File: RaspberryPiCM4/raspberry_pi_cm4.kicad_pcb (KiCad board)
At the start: 2 copper layers, 24 parts, among them J1 CONN_2x50_FEM_RPI_CM4_1-100, J2 CONN_2x50_FEM_RPI_CM4_101_200, U1 74LVC1G07_SOT353

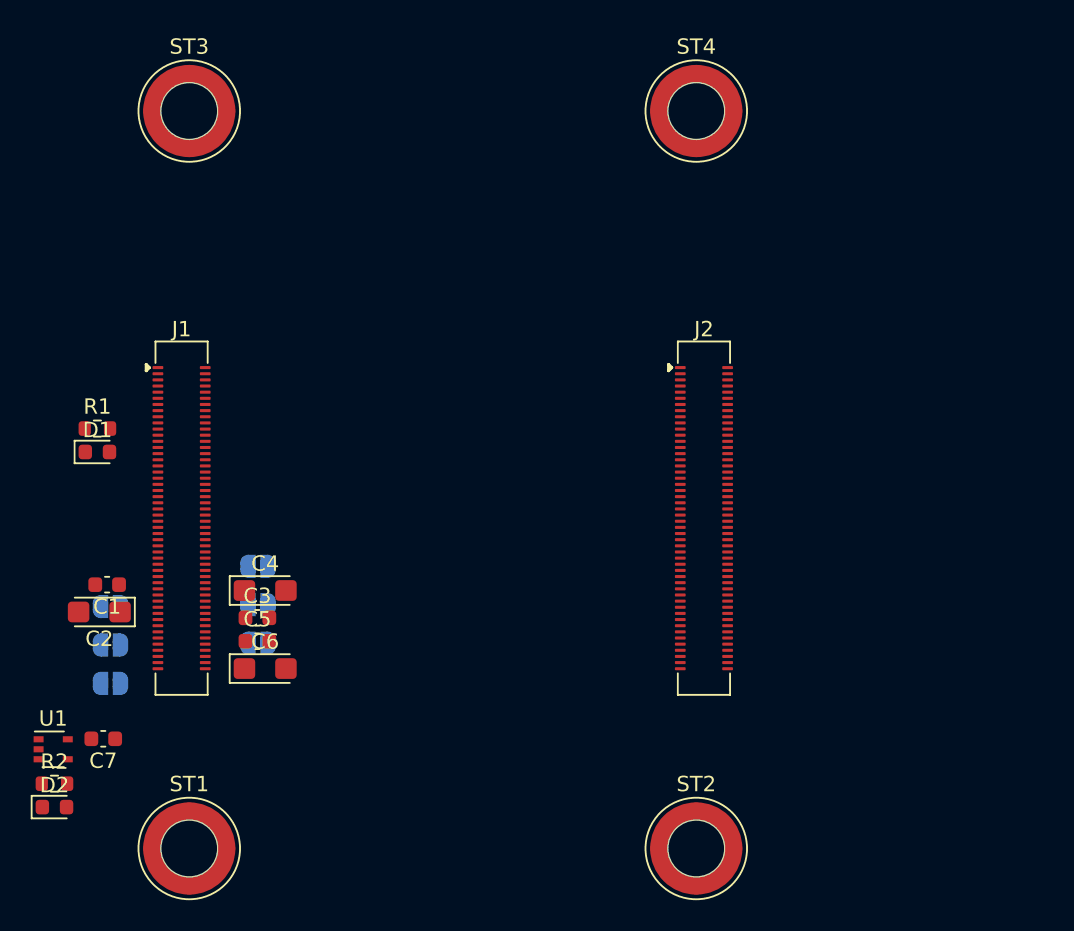
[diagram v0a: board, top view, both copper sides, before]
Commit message: migating to kicad 6
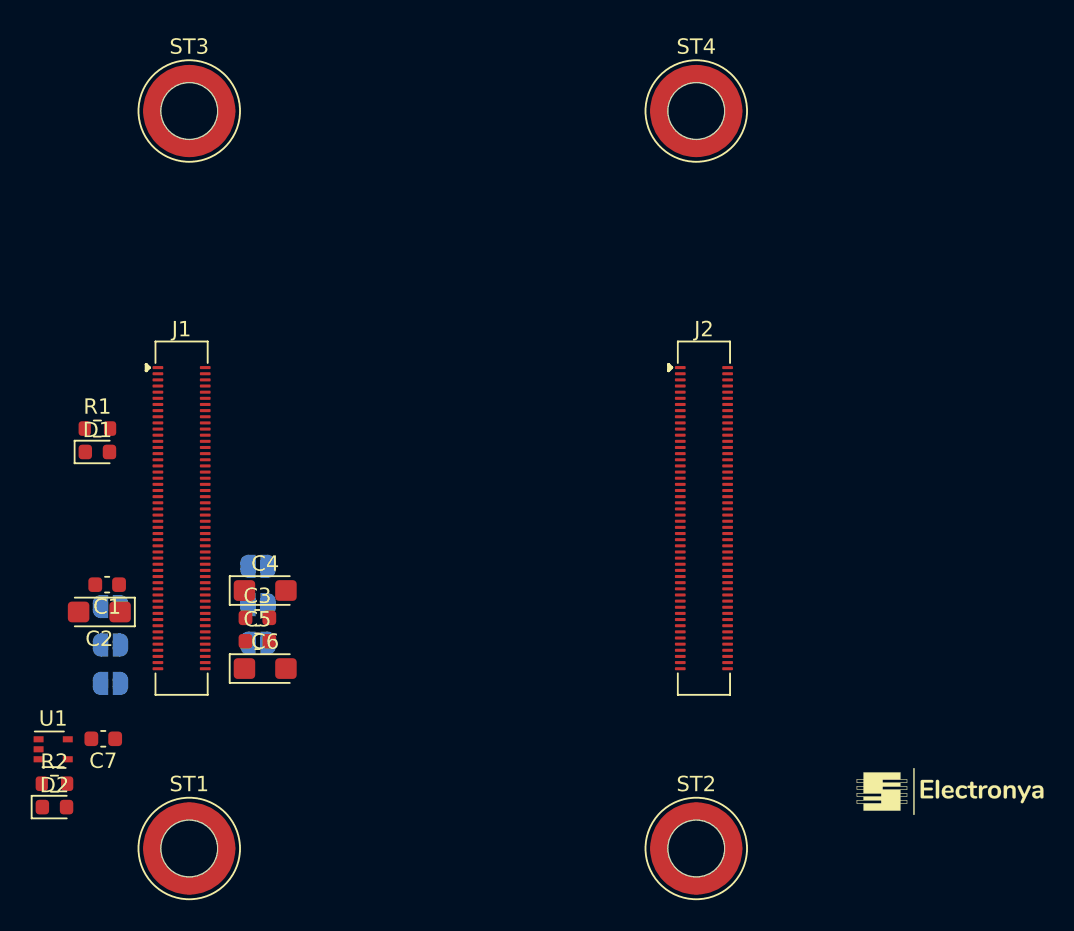
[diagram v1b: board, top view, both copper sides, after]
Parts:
- added G1: Electronya_Logo, ENYA_Bitmap:Electronya_Logo_12MM, F.Cu at (160.0, 97.8)
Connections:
- J1 pad 10: (no net) -> /GBE0_P
- J1 pad 100: (no net) -> /nEXT_RST
- J1 pad 12: (no net) -> /GBE0_N
- J1 pad 15: (no net) -> GND
- J1 pad 17: (no net) -> /nGBE_100_1G
- J1 pad 18: (no net) -> /GBE_SYNC_OUT
- J1 pad 19: (no net) -> /nGBE_10_1G
- J1 pad 20: (no net) -> /nID_WP
- J1 pad 21: /nPI_ACT -> GND
- J1 pad 24: (no net) -> /GPIO26
- J1 pad 25: (no net) -> GND
- J1 pad 26: (no net) -> /GPIO19
- J1 pad 27: (no net) -> /GPIO20
- J1 pad 28: (no net) -> /GPIO13
- J1 pad 29: (no net) -> /GPIO16
- J1 pad 30: (no net) -> /GPIO6
- J1 pad 31: (no net) -> /GPIO12
- J1 pad 34: (no net) -> /GPIO5
- J1 pad 35: (no net) -> /ID_SCL
- J1 pad 36: (no net) -> /ID_SDA
- J1 pad 37: (no net) -> /GPIO7
- J1 pad 38: (no net) -> /GPIO11
- J1 pad 39: (no net) -> /GPIO8
- J1 pad 4: (no net) -> /GBE1_P
- J1 pad 40: (no net) -> /GPIO9
- J1 pad 41: (no net) -> /GPIO25
- J1 pad 44: (no net) -> /GPIO10
- J1 pad 45: (no net) -> /GPIO24
- J1 pad 46: (no net) -> /GPIO22
- J1 pad 47: (no net) -> /GPIO23
- J1 pad 48: (no net) -> /GPIO27
- J1 pad 49: (no net) -> /GPIO18
- J1 pad 50: (no net) -> /GPIO17
- J1 pad 51: (no net) -> /GPIO15
- J1 pad 54: (no net) -> /GPIO4
- J1 pad 55: (no net) -> /GPIO14
- J1 pad 56: (no net) -> /GPIO3
- J1 pad 57: (no net) -> /SD_CLK
- J1 pad 58: (no net) -> /GPIO2
- J1 pad 6: (no net) -> /GBE1_N
- J1 pad 61: (no net) -> /SD_DAT3
- J1 pad 62: (no net) -> /SD_CMD
- J1 pad 63: (no net) -> /SD_DAT0
- J1 pad 64: (no net) -> /SD_DAT5
- J1 pad 67: (no net) -> /SD_DAT1
- J1 pad 68: (no net) -> /SD_DAT4
- J1 pad 69: (no net) -> /SD_DAT2
- J1 pad 70: (no net) -> /SD_DAT7
- J1 pad 72: (no net) -> /SD_DAT6
- J1 pad 73: (no net) -> /SD_VDD_OVRD
- J1 pad 75: (no net) -> /SD_PWR_ON
- J1 pad 76: (no net) -> unconnected-(J1-Pad76)
- J1 pad 80: (no net) -> /I2C0_SCL
- J1 pad 82: (no net) -> /I2C_SDA
- J1 pad 9: (no net) -> /GBE2_P
- J1 pad 94: (no net) -> /AN1
- J1 pad 96: (no net) -> /AN0
- J1 pad 97: (no net) -> /CAM_GPIO
- J1 pad 99: (no net) -> /GLOBAL_EN
- J2 pad 1: (no net) -> /USB_OTG_ID
- J2 pad 10: (no net) -> /PCIE_CLK_P
- J2 pad 100: (no net) -> /HDMI0_SCL
- J2 pad 11: (no net) -> /VDAC_COMP
- J2 pad 12: (no net) -> /PCIE_CLK_N
- J2 pad 15: (no net) -> /CAM1_D0_N
- J2 pad 16: (no net) -> /PCIE_RX_P
- J2 pad 17: (no net) -> /CAM1_D0_P
- J2 pad 18: (no net) -> /PCIE_RX_N
- J2 pad 2: (no net) -> /nPCIE_CLK_REQ
- J2 pad 21: (no net) -> /CAM1_D1_N
- J2 pad 22: (no net) -> /PCIE_TX_P
- J2 pad 23: (no net) -> /CAM1_D1_P
- J2 pad 24: (no net) -> /PCIE_TX_N
- J2 pad 27: (no net) -> /CAM1_CLK_N
- J2 pad 28: (no net) -> /CAM0_D0_N
- J2 pad 29: (no net) -> /CAM1_CLK_P
- J2 pad 3: (no net) -> /USB_D_N
- J2 pad 30: (no net) -> /CAM0_D0_P
- J2 pad 33: (no net) -> /CAM1_D2_N
- J2 pad 34: (no net) -> /CAM0_D1_N
- J2 pad 35: (no net) -> /CAM1_D2_P
- J2 pad 36: (no net) -> /CAM0_D1_P
- J2 pad 39: (no net) -> /CAM1_D3_N
- J2 pad 4: (no net) -> unconnected-(J2-Pad4)
- J2 pad 40: (no net) -> /CAM0_CLK_N
- J2 pad 41: (no net) -> /CAM1_D3_P
- J2 pad 42: (no net) -> /CAM0_CLK_P
- J2 pad 43: (no net) -> /HDMI1_HP
- J2 pad 45: (no net) -> /HDMI1_SDA
- J2 pad 46: (no net) -> /HDMI1_TX2_P
- J2 pad 47: (no net) -> /HDMI1_SCL
- J2 pad 48: (no net) -> /HDMI1_TX2_N
- J2 pad 49: (no net) -> /HDMI1_CEC
- J2 pad 5: (no net) -> /USB_D_P
- J2 pad 51: (no net) -> /HDMI0_CEC
- J2 pad 52: (no net) -> /HDMI1_TX1_P
- J2 pad 53: (no net) -> /HDMI0_HP
- J2 pad 54: (no net) -> /HDMI1_TX1_N
- J2 pad 57: (no net) -> /DSI0_D0_N
- J2 pad 58: (no net) -> /HDMI1_TX0_P
- J2 pad 59: (no net) -> /DSI0_D0_P
- J2 pad 6: (no net) -> unconnected-(J2-Pad6)
- J2 pad 60: (no net) -> /HDMI1_TX0_N
- J2 pad 63: (no net) -> /DSI0_D1_N
- J2 pad 64: (no net) -> /HDMI1_CLK_P
- J2 pad 65: (no net) -> /DSI0_D1_P
- J2 pad 66: (no net) -> /HDMI1_CLK_N
- J2 pad 69: (no net) -> /DSI0_CLK_N
- J2 pad 70: (no net) -> /HDMI0_TX2_P
- J2 pad 71: (no net) -> /DSI0_CLK_P
- J2 pad 72: (no net) -> /HDMI0_TX2_N
- J2 pad 75: (no net) -> /DSI1_D0_N
- J2 pad 76: (no net) -> /HDMI0_TX1_P
- J2 pad 77: (no net) -> /DSI1_D0_P
- J2 pad 78: (no net) -> /HDMI0_TX1_N
- J2 pad 81: (no net) -> /DSI1_D1_N
- J2 pad 82: (no net) -> /HDMI0_TX0_P
- J2 pad 83: (no net) -> /DSI1_D1_P
- J2 pad 84: (no net) -> /HDMI0_TX0_N
- J2 pad 87: (no net) -> /DSI1_CLK_N
- J2 pad 88: (no net) -> /HDMI0_CLK_P
- J2 pad 89: (no net) -> /DSI1_CLK_P
- J2 pad 9: (no net) -> /nPCIE_RST
- J2 pad 90: (no net) -> /HDMI0_CLK_N
- J2 pad 93: (no net) -> /DSI1_D2_N
- J2 pad 94: (no net) -> /DSI1_D3_N
- J2 pad 95: (no net) -> /DSI1_D2_P
- J2 pad 96: (no net) -> /DSI1_D3_P
- J2 pad 99: (no net) -> /HDMI0_SDA
- R1 pad 2: /nPI_ACT -> GND
- ST1 pad 1: Net-(ST1-Pad1) -> unconnected-(ST1-Pad1)
- ST2 pad 1: Net-(ST2-Pad1) -> unconnected-(ST2-Pad1)
- ST3 pad 1: Net-(ST3-Pad1) -> unconnected-(ST3-Pad1)
- ST4 pad 1: Net-(ST4-Pad1) -> unconnected-(ST4-Pad1)
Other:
- net class Default removed
- net class PWR removed
